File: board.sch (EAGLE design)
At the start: 87 parts, among them J1 AVR_SPI_PRG_6NS, U1 TPS2112A, U2 MAX1555, U3 USD-SOCKETNEW, U4 3.3V, U5 2.8V, U6 74HC595, Y1 8MHz, Y2 12.288MHz

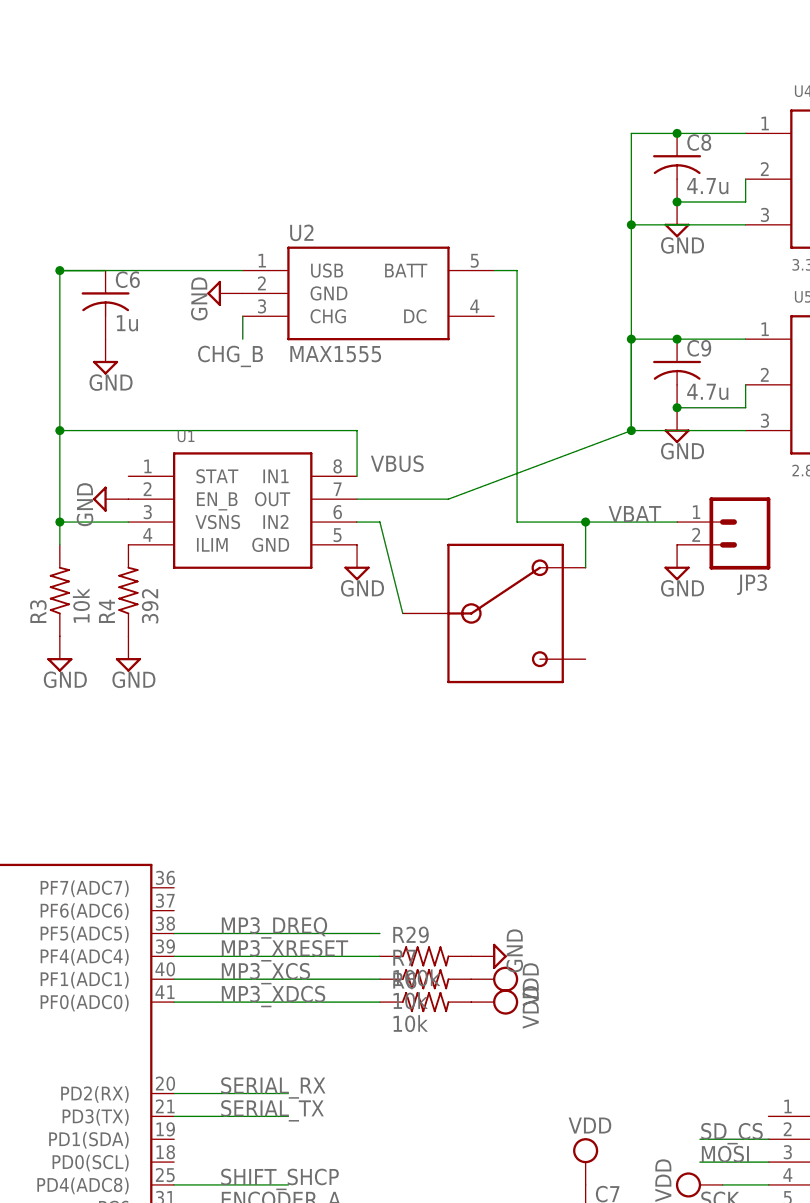
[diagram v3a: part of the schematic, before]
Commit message: Added battery sense, updated revision, and centered LEDs
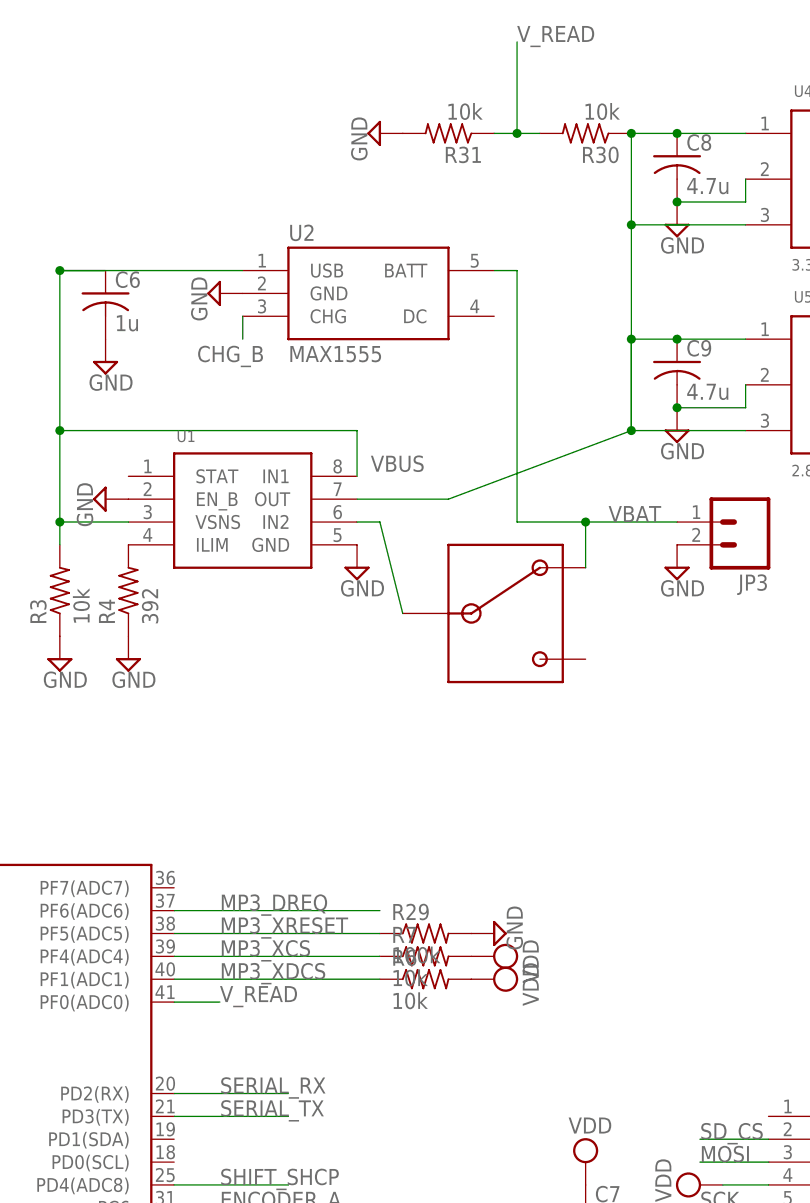
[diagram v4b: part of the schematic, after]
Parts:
- added R30, R31: 10k, rcl:R-US_R0603
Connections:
- new net V_READ: R30.2, R31.1, U$1.PF0(ADC0)
- net GND: now also R31.2
- net MP3_DREQ: now also U$1.PF6(ADC6); no longer U$1.PF5(ADC5)
- net MP3_XCS: now also U$1.PF4(ADC4); no longer U$1.PF1(ADC1)
- net MP3_XDCS: now also U$1.PF1(ADC1); no longer U$1.PF0(ADC0)
- net MP3_XRESET: now also U$1.PF5(ADC5); no longer U$1.PF4(ADC4)
- net N$18: now also R30.1
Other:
- moved on the sheet: R29, R6, R7
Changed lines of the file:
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@@
 <part name="SUPPLY53" library="supply2" deviceset="VDD" device=""/>
 <part name="C31" library="rcl" deviceset="C-US" device="C0603K" value="0.1u"/>
+<part name="R30" library="rcl" deviceset="R-US_" device="R0603" value="10k"/>
+<part name="R31" library="rcl" deviceset="R-US_" device="R0603" value="10k"/>
+<part name="SUPPLY54" library="supply2" deviceset="GND" device=""/>
 </parts>
 <sheets>
@@
 <instance part="R13" gate="G$1" x="187.96" y="27.94" rot="R90"/>
 <instance part="SUPPLY10" gate="GND" x="180.34" y="20.32"/>
-<instance part="R7" gate="G$1" x="93.98" y="91.44"/>
+<instance part="R7" gate="G$1" x="93.98" y="93.98"/>
 <instance part="R8" gate="G$1" x="83.82" y="43.18"/>
-<instance part="R6" gate="G$1" x="93.98" y="88.9"/>
-<instance part="SUPPLY14" gate="G$1" x="101.6" y="88.9" rot="R270"/>
-<instance part="SUPPLY19" gate="G$1" x="101.6" y="91.44" rot="R270"/>
+<instance part="R6" gate="G$1" x="93.98" y="91.44"/>
+<instance part="SUPPLY14" gate="G$1" x="101.6" y="91.44" rot="R270"/>
+<instance part="SUPPLY19" gate="G$1" x="101.6" y="93.98" rot="R270"/>
 <instance part="SUPPLY52" gate="G$1" x="93.98" y="43.18" rot="R270"/>
-<instance part="R29" gate="G$1" x="93.98" y="93.98"/>
-<instance part="SUPPLY34" gate="GND" x="101.6" y="93.98" rot="R90"/>
+<instance part="R29" gate="G$1" x="93.98" y="96.52"/>
+<instance part="SUPPLY34" gate="GND" x="101.6" y="96.52" rot="R90"/>
 <instance part="U$1" gate="G$1" x="48.26" y="66.04"/>
 <instance part="SUPPLY53" gate="G$1" x="27.94" y="99.06" rot="R90"/>
 <instance part="C31" gate="G$1" x="7.62" y="33.02"/>
+<instance part="R30" gate="G$1" x="111.76" y="185.42" rot="R180"/>
+<instance part="R31" gate="G$1" x="96.52" y="185.42" rot="R180"/>
+<instance part="SUPPLY54" gate="GND" x="88.9" y="185.42" rot="R270"/>
 </instances>
 <busses>
@@
 <wire x1="30.48" y1="35.56" x2="30.48" y2="38.1" width="0.1524" layer="91"/>
 <junction x="30.48" y="35.56"/>
+</segment>
+<segment>
+<pinref part="R31" gate="G$1" pin="2"/>
+<pinref part="SUPPLY54" gate="GND" pin="GND"/>
 </segment>
 </net>
@@
 <pinref part="U5" gate="G$1" pin="EN"/>
 <wire x1="116.84" y1="152.4" x2="129.54" y2="152.4" width="0.1524" layer="91"/>
+<pinref part="R30" gate="G$1" pin="1"/>
+<junction x="116.84" y="185.42"/>
 </segment>
 </net>
@@
 <net name="MP3_XCS" class="0">
 <segment>
-<label x="71.12" y="91.44" size="1.778" layer="95"/>
+<label x="71.12" y="93.98" size="1.778" layer="95"/>
 <pinref part="R7" gate="G$1" pin="1"/>
-<wire x1="88.9" y1="91.44" x2="66.04" y2="91.44" width="0.1524" layer="91"/>
-<pinref part="U$1" gate="G$1" pin="PF1(ADC1)"/>
+<wire x1="88.9" y1="93.98" x2="66.04" y2="93.98" width="0.1524" layer="91"/>
+<pinref part="U$1" gate="G$1" pin="PF4(ADC4)"/>
 </segment>
 <segment>
@@
 </segment>
 <segment>
-<wire x1="66.04" y1="88.9" x2="88.9" y2="88.9" width="0.1524" layer="91"/>
-<label x="71.12" y="88.9" size="1.778" layer="95"/>
+<label x="71.12" y="91.44" size="1.778" layer="95"/>
 <pinref part="R6" gate="G$1" pin="1"/>
-<pinref part="U$1" gate="G$1" pin="PF0(ADC0)"/>
+<pinref part="U$1" gate="G$1" pin="PF1(ADC1)"/>
+<wire x1="66.04" y1="91.44" x2="88.9" y2="91.44" width="0.1524" layer="91"/>
 </segment>
 </net>
@@
 </segment>
 <segment>
-<label x="71.12" y="96.52" size="1.778" layer="95"/>
-<pinref part="U$1" gate="G$1" pin="PF5(ADC5)"/>
-<wire x1="88.9" y1="96.52" x2="66.04" y2="96.52" width="0.1524" layer="91"/>
+<label x="71.12" y="99.06" size="1.778" layer="95"/>
+<wire x1="88.9" y1="99.06" x2="66.04" y2="99.06" width="0.1524" layer="91"/>
+<pinref part="U$1" gate="G$1" pin="PF6(ADC6)"/>
 </segment>
 </net>
@@
 </segment>
 <segment>
-<label x="71.12" y="93.98" size="1.778" layer="95"/>
-<wire x1="66.04" y1="93.98" x2="88.9" y2="93.98" width="0.1524" layer="91"/>
+<label x="71.12" y="96.52" size="1.778" layer="95"/>
 <pinref part="R29" gate="G$1" pin="1"/>
-<pinref part="U$1" gate="G$1" pin="PF4(ADC4)"/>
+<pinref part="U$1" gate="G$1" pin="PF5(ADC5)"/>
+<wire x1="66.04" y1="96.52" x2="88.9" y2="96.52" width="0.1524" layer="91"/>
 </segment>
 </net>
@@
 </segment>
 </net>
+<net name="V_READ" class="0">
+<segment>
+<pinref part="R30" gate="G$1" pin="2"/>
+<pinref part="R31" gate="G$1" pin="1"/>
+<wire x1="101.6" y1="185.42" x2="104.14" y2="185.42" width="0.1524" layer="91"/>
+<wire x1="104.14" y1="185.42" x2="106.68" y2="185.42" width="0.1524" layer="91"/>
+<wire x1="104.14" y1="185.42" x2="104.14" y2="195.58" width="0.1524" layer="91"/>
+<junction x="104.14" y="185.42"/>
+<label x="104.14" y="195.58" size="1.778" layer="95"/>
+</segment>
+<segment>
+<pinref part="U$1" gate="G$1" pin="PF0(ADC0)"/>
+<wire x1="66.04" y1="88.9" x2="71.12" y2="88.9" width="0.1524" layer="91"/>
+<label x="71.12" y="88.9" size="1.778" layer="95"/>
+</segment>
+</net>

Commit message: More board cleanup
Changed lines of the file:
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@@
 <segment>
 <label x="71.12" y="60.96" size="1.778" layer="95"/>
-<wire x1="66.04" y1="60.96" x2="76.2" y2="60.96" width="0.1524" layer="91"/>
+<wire x1="66.04" y1="60.96" x2="78.74" y2="60.96" width="0.1524" layer="91"/>
 <pinref part="U$1" gate="G$1" pin="PE6"/>
 </segment>
@@
 <segment>
 <label x="71.12" y="99.06" size="1.778" layer="95"/>
-<wire x1="88.9" y1="99.06" x2="66.04" y2="99.06" width="0.1524" layer="91"/>
+<wire x1="78.74" y1="99.06" x2="66.04" y2="99.06" width="0.1524" layer="91"/>
 <pinref part="U$1" gate="G$1" pin="PF6(ADC6)"/>
 </segment>
@@
 <segment>
 <pinref part="U$1" gate="G$1" pin="PF0(ADC0)"/>
-<wire x1="66.04" y1="88.9" x2="71.12" y2="88.9" width="0.1524" layer="91"/>
+<wire x1="66.04" y1="88.9" x2="78.74" y2="88.9" width="0.1524" layer="91"/>
 <label x="71.12" y="88.9" size="1.778" layer="95"/>
 </segment>

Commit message: Move switch to be flush with board
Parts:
- C25: value 0.1u -> 1u
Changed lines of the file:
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@@
 <part name="J1" library="SparkFun-Connectors" deviceset="AVR_SPI_PRG_6" device="NS"/>
 <part name="JP2" library="SparkFun-Connectors" deviceset="ARDUINO_SERIAL_PROGRAM" device="LOCK"/>
-<part name="C25" library="rcl" deviceset="C-US" device="C0603K" value="0.1u"/>
+<part name="C25" library="rcl" deviceset="C-US" device="C0603K" value="1u"/>
 <part name="SUPPLY1" library="supply2" deviceset="VDD" device=""/>
 <part name="C24" library="rcl" deviceset="C-US" device="C0603K" value="0.1u"/>

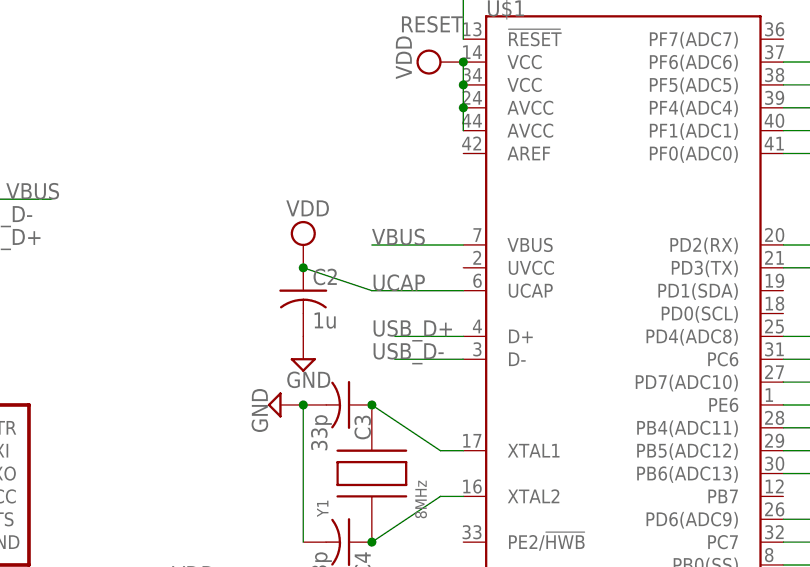
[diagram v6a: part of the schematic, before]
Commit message: Why wasn't UCAP connected to VDD?
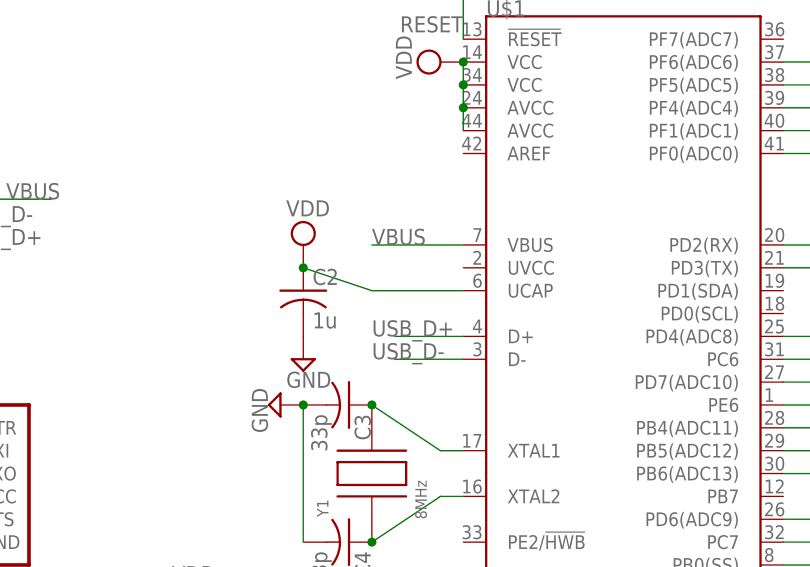
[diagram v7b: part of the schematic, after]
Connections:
- removed net UCAP: C2.1, U$1.UCAP
- net VDD: now also C2.1, U$1.UCAP
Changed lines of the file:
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@@
 <part name="SUPPLY51" library="supply2" deviceset="VDD" device=""/>
 <part name="C17" library="rcl" deviceset="C-US" device="C0603K" value="1u"/>
-<part name="SUPPLY40" library="supply2" deviceset="VDD" device=""/>
 <part name="SUPPLY41" library="supply2" deviceset="GND" device=""/>
 <part name="SUPPLY57" library="supply2" deviceset="GND" device=""/>
@@
 <part name="R31" library="rcl" deviceset="R-US_" device="R0603" value="10k"/>
 <part name="SUPPLY54" library="supply2" deviceset="GND" device=""/>
+<part name="SUPPLY40" library="supply2" deviceset="VDD" device=""/>
 </parts>
 <sheets>
@@
 <instance part="SUPPLY51" gate="G$1" x="30.48" y="119.38"/>
 <instance part="C17" gate="G$1" x="218.44" y="132.08" rot="R270"/>
-<instance part="SUPPLY40" gate="G$1" x="12.7" y="78.74"/>
 <instance part="SUPPLY41" gate="GND" x="0" y="25.4"/>
 <instance part="SUPPLY57" gate="GND" x="27.94" y="27.94" rot="R270"/>
@@
 <instance part="R31" gate="G$1" x="96.52" y="185.42" rot="R180"/>
 <instance part="SUPPLY54" gate="GND" x="88.9" y="185.42" rot="R270"/>
+<instance part="SUPPLY40" gate="G$1" x="12.7" y="78.74"/>
 </instances>
 <busses>
@@
 <wire x1="30.48" y1="93.98" x2="30.48" y2="91.44" width="0.1524" layer="91"/>
 <junction x="30.48" y="93.98"/>
+</segment>
+<segment>
+<pinref part="C2" gate="G$1" pin="1"/>
+<wire x1="20.32" y1="73.66" x2="12.7" y2="76.2" width="0.1524" layer="91"/>
+<pinref part="U$1" gate="G$1" pin="UCAP"/>
+<wire x1="30.48" y1="73.66" x2="20.32" y2="73.66" width="0.1524" layer="91"/>
+<pinref part="SUPPLY40" gate="G$1" pin="VDD"/>
+<junction x="12.7" y="76.2"/>
 </segment>
 </net>
@@
 </segment>
 </net>
-<net name="UCAP" class="0">
-<segment>
-<pinref part="C2" gate="G$1" pin="1"/>
-<pinref part="SUPPLY40" gate="G$1" pin="VDD"/>
-<wire x1="20.32" y1="73.66" x2="12.7" y2="76.2" width="0.1524" layer="91"/>
-<junction x="12.7" y="76.2"/>
-<pinref part="U$1" gate="G$1" pin="UCAP"/>
-<wire x1="30.48" y1="73.66" x2="20.32" y2="73.66" width="0.1524" layer="91"/>
-<label x="20.32" y="73.66" size="1.778" layer="95"/>
-</segment>
-</net>
